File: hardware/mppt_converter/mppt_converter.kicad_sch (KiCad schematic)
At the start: 62 parts, among them J101 CT3151, J102 CT3151, J103 CT3151, J104 CT3151, Q101 EPC2059, Q102 EPC2059, Q103 BSS127S, U101 ADUM4221-1ARIZ

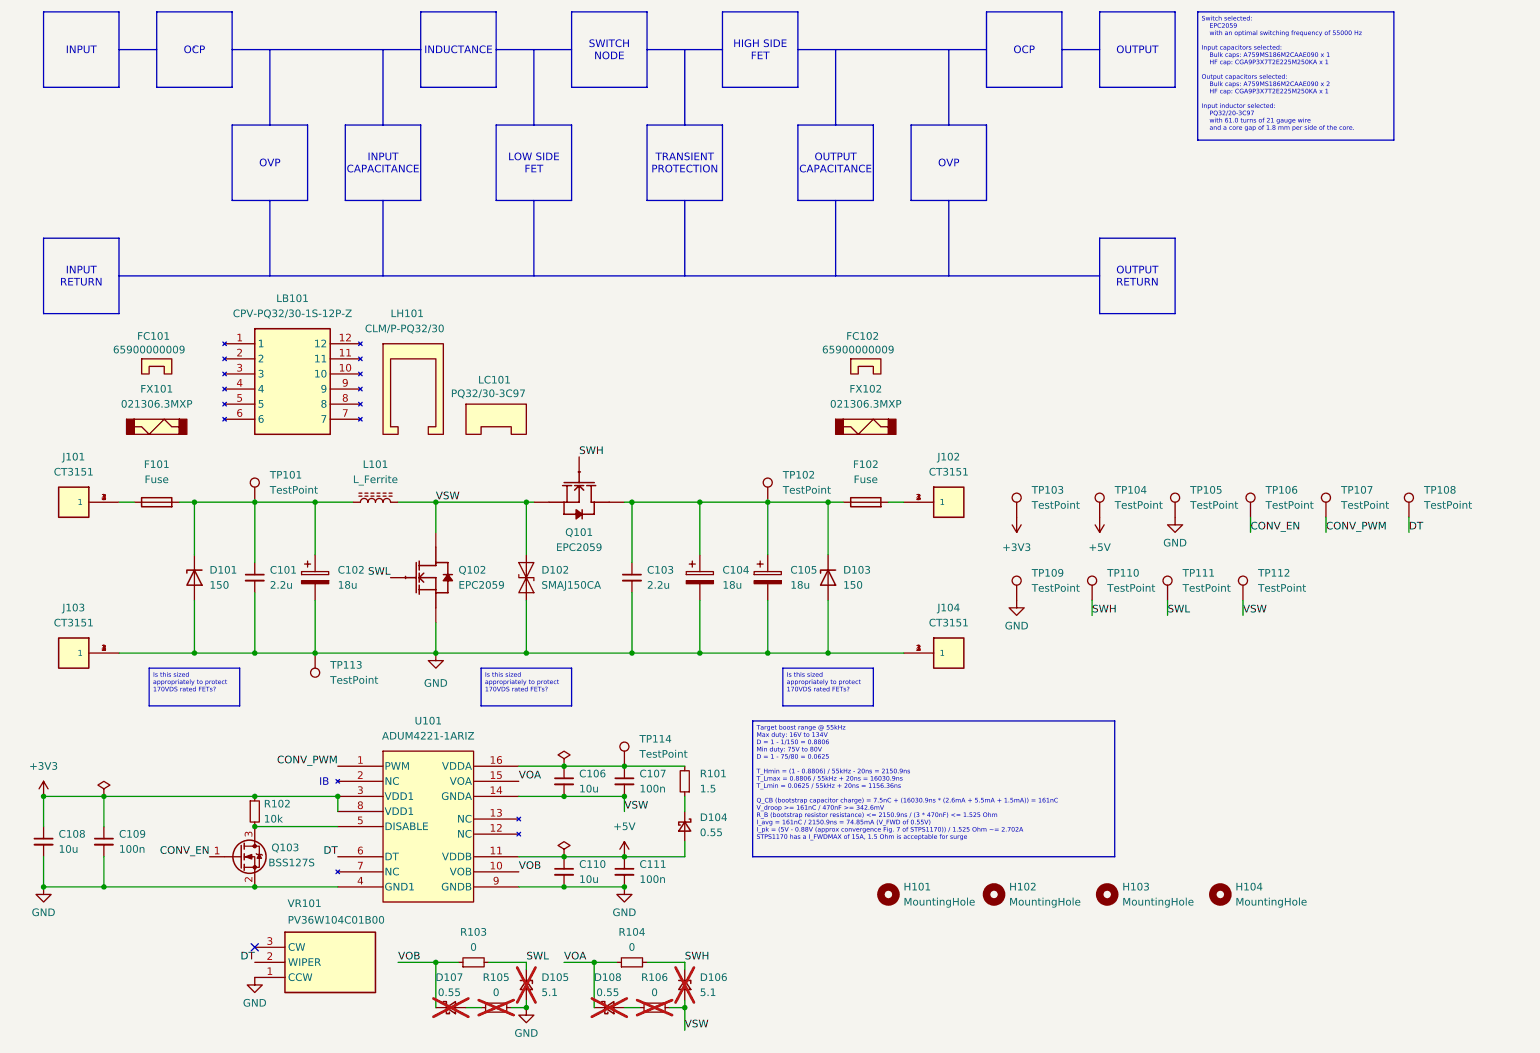
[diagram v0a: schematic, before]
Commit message: changed layout of switching loop planes, added small 100n capacitors on HV input and output
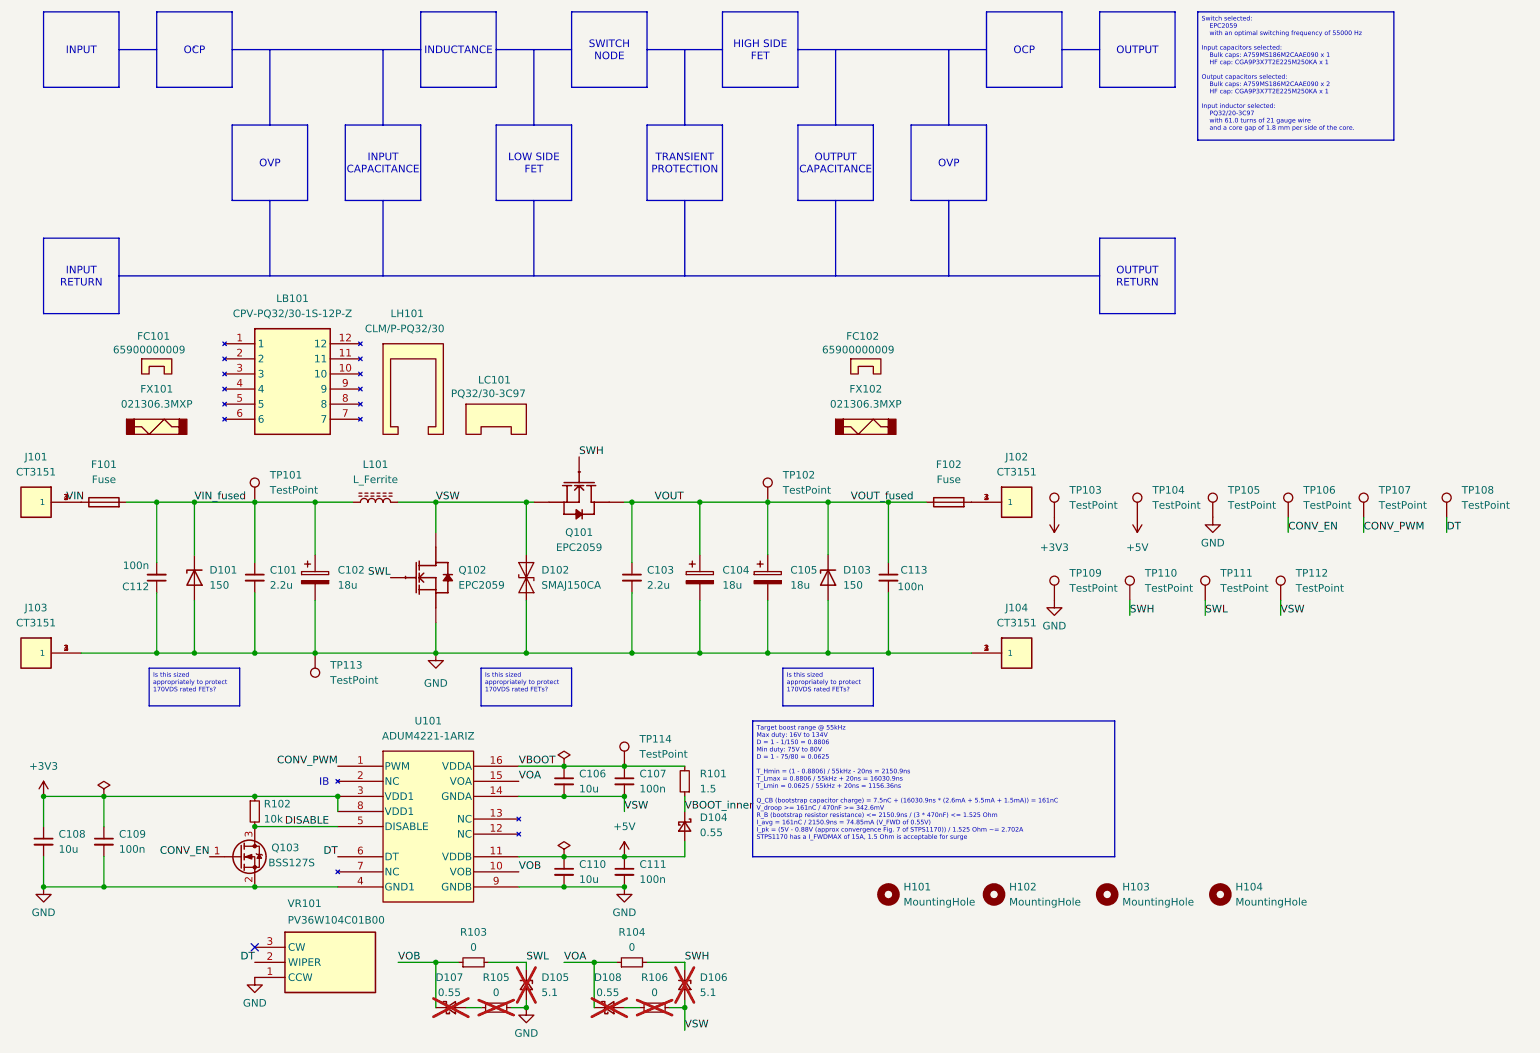
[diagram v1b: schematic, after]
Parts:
- added C112, C113: 100n, Capacitor_SMD:C_0805_2012Metric_Pad1.18x1.45mm_HandSolder, symbol Device:C_Small
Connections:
- net GND: now also C112.1, C113.2
- net VIN_fused: now reaches C101.1, C102.1, D101.1 (K), F101.2, L101.1, TP101.1
- net VIN_fused: now also C112.2
- net VBOOT: now reaches C106.1, C107.1, R101.2, TP114.1, U101.16 (VDDA)
- net DISABLE: now reaches Q103.3 (D), R102.2, U101.5 (DISABLE)
- net VOUT: now reaches C103.1, C104.1, C105.1, D103.1 (K), F102.1, Q101.3 (D), Q101.5 (D), TP102.1
- net VOUT: now also C113.1
- net VBOOT_inner: now reaches D104.1 (K), R101.1
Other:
- moved on the sheet: F101, F102, J101, J102, J103, J104, TP103, TP104, TP105, TP106, TP107, TP108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
